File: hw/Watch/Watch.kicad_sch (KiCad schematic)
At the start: 8 parts, among them J3 Conn_01x02, J4 Conn_01x02, J5 Conn_01x02, J6 Conn_01x02

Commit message: wip
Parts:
- removed J3, J4, J5, J6: Conn_01x02, symbol Connector_Generic:Conn_01x02
- added J3: Conn_01x04, RKL-Connectors:FFC-FPC_1x04_0.5mm, symbol Connector_Generic:Conn_01x04
- added J8: Conn_01x04, RKL-Connectors:FFC-FPC_1x04_0.5mm_cable, symbol Connector_Generic:Conn_01x04
- C27, C28: footprint Capacitor_SMD:C_0402_1005Metric -> Capacitor_SMD:C_0201_0603Metric; Basic/Extended B -> E; LCSC C1523 -> C66942
- L2, L3: footprint RKL-Inductors:PCB_coil -> RKL-Inductors:PCB_coil_linear_N24
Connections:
- net MainBoard/LC-0A: now also J3.1 (Pin_1)
- net MainBoard/LC-0B: now also J3.2 (Pin_2)
- net MainBoard/LC-1A: now also J3.3 (Pin_3)
- net MainBoard/LC-1B: now also J3.4 (Pin_4)
- net at L3.1: now also J8.3 (Pin_3)
- net at L3.2: now also J8.4 (Pin_4)
- net at L2.1: now also J8.1 (Pin_1)
- net at L2.2: now also J8.2 (Pin_2)
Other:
- moved on the sheet: C27, C28, L2, L3

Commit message: PCB
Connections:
- net at L3.1: now also J8.2 (Pin_2); no longer J8.3 (Pin_3)
- net at L3.2: now also J8.1 (Pin_1); no longer J8.4 (Pin_4)
- net at L2.1: now also J8.4 (Pin_4); no longer J8.1 (Pin_1)
- net at L2.2: now also J8.3 (Pin_3); no longer J8.2 (Pin_2)
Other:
- moved on the sheet: L2, L3
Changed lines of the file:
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@@
     )
   )
-  (symbol (lib_id "Device:L") (at 99.06 97.79 0) (mirror y) (unit 1)
+  (symbol (lib_id "Device:L") (at 99.06 82.55 180) (unit 1)
     (in_bom yes) (on_board yes) (dnp no)
-    (property "Reference" "L3" (at 100.33 96.52 0)
+    (property "Reference" "L3" (at 100.33 83.82 0)
       (effects (font (size 1.27 1.27)) (justify right))
     )
-    (property "Value" "L" (at 100.33 99.06 0)
+    (property "Value" "L" (at 100.33 81.28 0)
       (effects (font (size 1.27 1.27)) (justify right))
     )
-    (property "Footprint" "RKL-Inductors:PCB_coil_linear_N24" (at 99.06 97.79 0)
+    (property "Footprint" "RKL-Inductors:PCB_coil_linear_N24" (at 99.06 82.55 0)
       (effects (font (size 1.27 1.27)) hide)
     )
-    (property "Datasheet" "~" (at 99.06 97.79 0)
+    (property "Datasheet" "~" (at 99.06 82.55 0)
       (effects (font (size 1.27 1.27)) hide)
     )
-    (property "JLCPCB_IGNORE" "ignore" (at 99.06 97.79 0)
+    (property "JLCPCB_IGNORE" "ignore" (at 99.06 82.55 0)
       (effects (font (size 1.27 1.27)) hide)
     )
@@
     )
   )
-  (symbol (lib_id "Device:L") (at 99.06 82.55 0) (mirror y) (unit 1)
+  (symbol (lib_id "Device:L") (at 99.06 97.79 180) (unit 1)
     (in_bom yes) (on_board yes) (dnp no)
-    (property "Reference" "L2" (at 100.33 81.28 0)
+    (property "Reference" "L2" (at 100.33 99.06 0)
       (effects (font (size 1.27 1.27)) (justify right))
     )
-    (property "Value" "L" (at 100.33 83.82 0)
+    (property "Value" "L" (at 100.33 96.52 0)
       (effects (font (size 1.27 1.27)) (justify right))
     )
-    (property "Footprint" "RKL-Inductors:PCB_coil_linear_N24" (at 99.06 82.55 0)
+    (property "Footprint" "RKL-Inductors:PCB_coil_linear_N24" (at 99.06 97.79 0)
       (effects (font (size 1.27 1.27)) hide)
     )
-    (property "Datasheet" "~" (at 99.06 82.55 0)
+    (property "Datasheet" "~" (at 99.06 97.79 0)
       (effects (font (size 1.27 1.27)) hide)
     )
-    (property "JLCPCB_IGNORE" "ignore" (at 99.06 82.55 0)
+    (property "JLCPCB_IGNORE" "ignore" (at 99.06 97.79 0)
       (effects (font (size 1.27 1.27)) hide)
     )

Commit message: PCB v0.0.0
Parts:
- renumbered L3 to L1
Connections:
- net L1B: now reaches J8.2 (Pin_2), L1.1
- net L1A: now reaches J8.1 (Pin_1), L1.2
- net L2B: now reaches J8.4 (Pin_4), L2.1
- net L2A: now reaches J8.3 (Pin_3), L2.2
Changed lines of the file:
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@@
     (effects (font (size 1.5 1.5) (thickness 0.3) bold) (justify left bottom))
+  )
+  (label "L1B" (at 107.95 88.9 0) (fields_autoplaced)
+    (effects (font (size 1.27 1.27)) (justify left bottom))
+  )
+  (label "L1A" (at 107.95 86.36 0) (fields_autoplaced)
+    (effects (font (size 1.27 1.27)) (justify left bottom))
+  )
+  (label "L2A" (at 107.95 91.44 0) (fields_autoplaced)
+    (effects (font (size 1.27 1.27)) (justify left bottom))
+  )
+  (label "L2B" (at 107.95 93.98 0) (fields_autoplaced)
+    (effects (font (size 1.27 1.27)) (justify left bottom))
   )
   (symbol (lib_id "Connector_Generic:Conn_01x04") (at 124.46 88.9 0) (mirror y) (unit 1)
@@
   (symbol (lib_id "Device:L") (at 99.06 82.55 180) (unit 1)
     (in_bom yes) (on_board yes) (dnp no)
-    (property "Reference" "L3" (at 100.33 83.82 0)
+    (property "Reference" "L1" (at 100.33 83.82 0)
       (effects (font (size 1.27 1.27)) (justify right))
     )
@@
       (project "Watch"
         (path "/1db6f6a7-b341-422f-8dcc-b4fd8e3ba0c0"
-          (reference "L3") (unit 1)
+          (reference "L1") (unit 1)
         )
       )

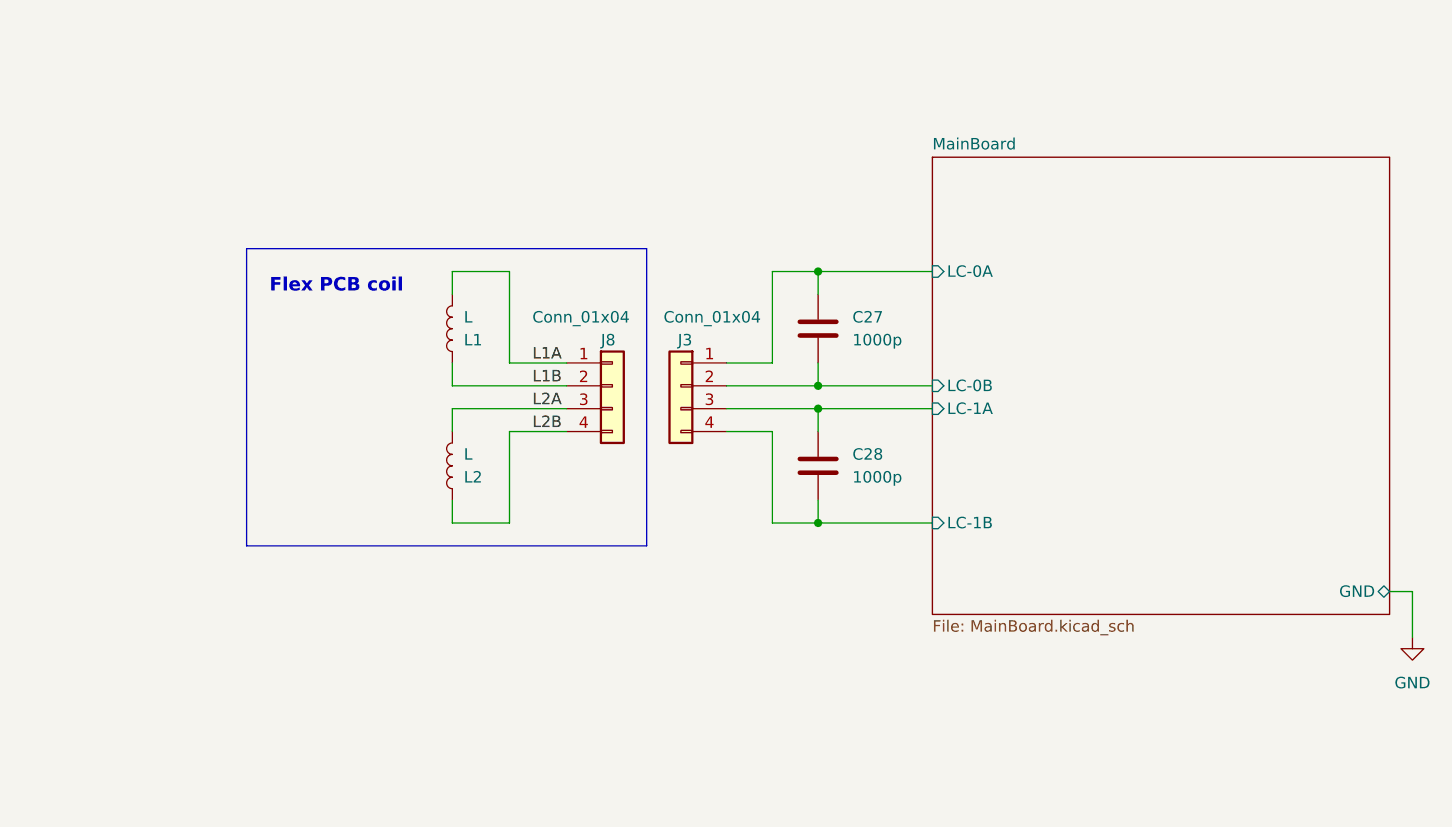
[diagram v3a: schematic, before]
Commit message: Shift LDO
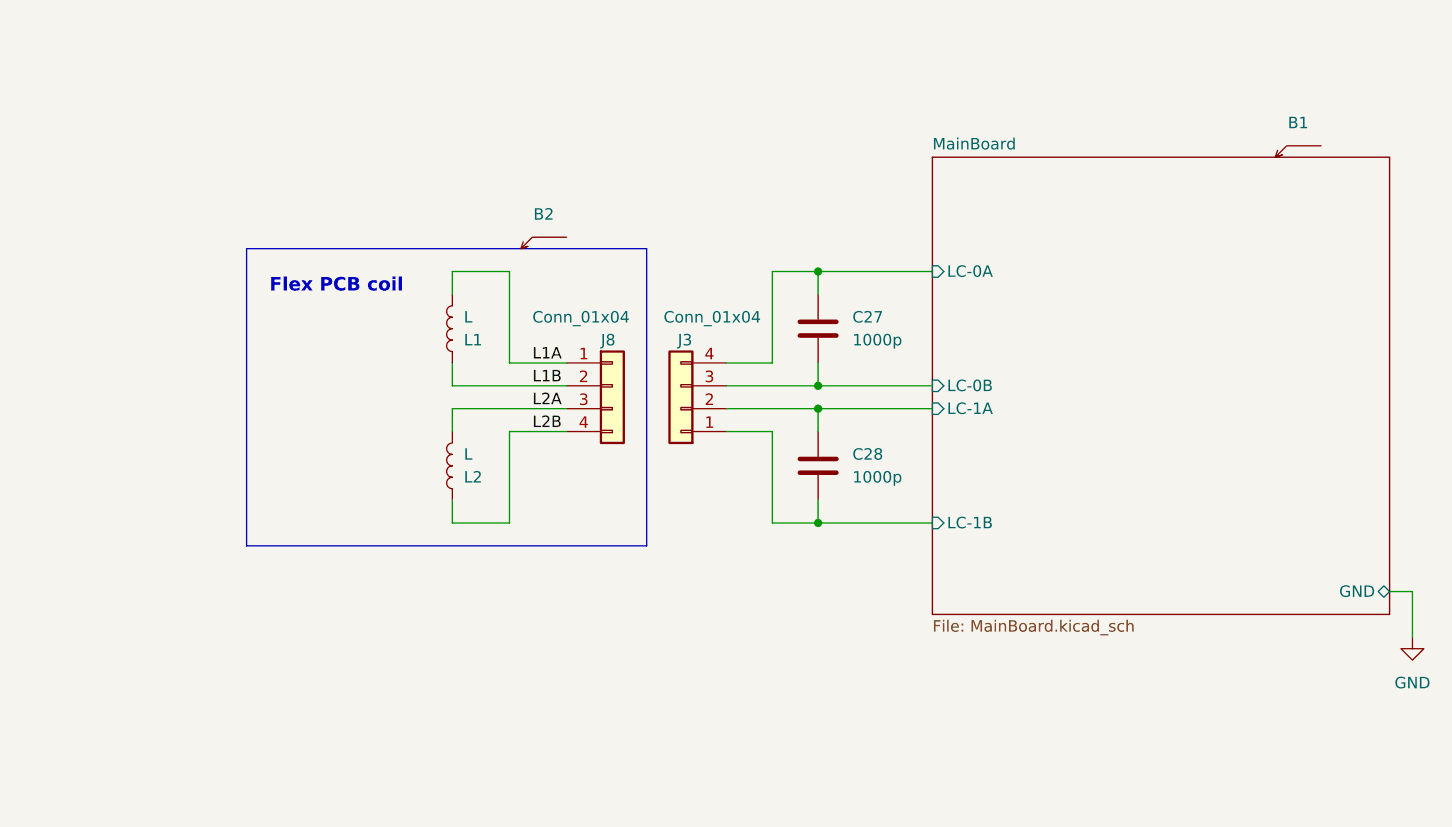
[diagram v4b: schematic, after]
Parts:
- added B1, B2: ~, RKL-AuxiliarySymbols:Board, symbol RKL-AuxiliarySymbols:Board
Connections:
- net MainBoard/LC-0A: now also J3.4 (Pin_4); no longer J3.1 (Pin_1)
- net MainBoard/LC-0B: now also J3.3 (Pin_3); no longer J3.2 (Pin_2)
- net MainBoard/LC-1A: now also J3.2 (Pin_2); no longer J3.3 (Pin_3)
- net MainBoard/LC-1B: now also J3.1 (Pin_1); no longer J3.4 (Pin_4)
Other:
- moved on the sheet: J3
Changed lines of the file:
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@@
     (effects (font (size 1.27 1.27)) (justify left bottom))
   )
-  (symbol (lib_id "Connector_Generic:Conn_01x04") (at 124.46 88.9 0) (mirror y) (unit 1)
+  (symbol (lib_id "Connector_Generic:Conn_01x04") (at 124.46 91.44 180) (unit 1)
     (in_bom yes) (on_board yes) (dnp no)
     (property "Reference" "J3" (at 125.73 83.82 0)
@@
       (effects (font (size 1.27 1.27)) (justify left))
     )
-    (property "Footprint" "RKL-Connectors:FFC-FPC_1x04_0.5mm" (at 124.46 88.9 0)
-      (effects (font (size 1.27 1.27)) hide)
-    )
-    (property "Datasheet" "~" (at 124.46 88.9 0)
+    (property "Footprint" "RKL-Connectors:FFC-FPC_1x04_0.5mm" (at 124.46 91.44 0)
+      (effects (font (size 1.27 1.27)) hide)
+    )
+    (property "Datasheet" "~" (at 124.46 91.44 0)
       (effects (font (size 1.27 1.27)) hide)
     )
@@
         (path "/1db6f6a7-b341-422f-8dcc-b4fd8e3ba0c0"
           (reference "J3") (unit 1)
+        )
+      )
+    )
+  )
+  (symbol (lib_id "RKL-AuxiliarySymbols:Board") (at 106.68 73.66 0) (unit 1)
+    (in_bom yes) (on_board yes) (dnp no) (fields_autoplaced)
+    (property "Reference" "B2" (at 109.22 69.85 0)
+      (effects (font (size 1.27 1.27)))
+    )
+    (property "Value" "~" (at 106.68 73.66 0)
+      (effects (font (size 1.27 1.27)))
+    )
+    (property "Footprint" "RKL-AuxiliarySymbols:Board" (at 109.22 68.58 0)
+      (effects (font (size 1.27 1.27)) hide)
+    )
+    (property "Datasheet" "" (at 106.68 73.66 0)
+      (effects (font (size 1.27 1.27)) hide)
+    )
+    (instances
+      (project "Watch"
+        (path "/1db6f6a7-b341-422f-8dcc-b4fd8e3ba0c0"
+          (reference "B2") (unit 1)
         )
       )
@@
         )
       )
+    )
+  )
+  (symbol (lib_id "RKL-AuxiliarySymbols:Board") (at 190.5 63.5 0) (unit 1)
+    (in_bom yes) (on_board yes) (dnp no) (fields_autoplaced)
+    (property "Reference" "B1" (at 193.04 59.69 0)
+      (effects (font (size 1.27 1.27)))
+    )
+    (property "Value" "~" (at 190.5 63.5 0)
+      (effects (font (size 1.27 1.27)))
+    )
+    (property "Footprint" "RKL-AuxiliarySymbols:Board" (at 193.04 58.42 0)
+      (effects (font (size 1.27 1.27)) hide)
+    )
+    (property "Datasheet" "" (at 190.5 63.5 0)
+      (effects (font (size 1.27 1.27)) hide)
+    )
+    (instances
+      (project "Watch"
+        (path "/1db6f6a7-b341-422f-8dcc-b4fd8e3ba0c0"
+          (reference "B1") (unit 1)
+        )
+      )

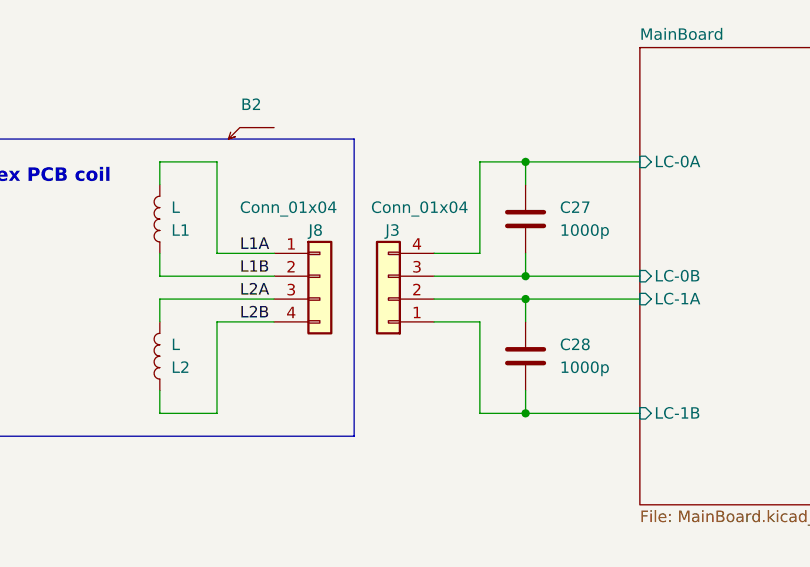
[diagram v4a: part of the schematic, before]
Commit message: Shift flex connector
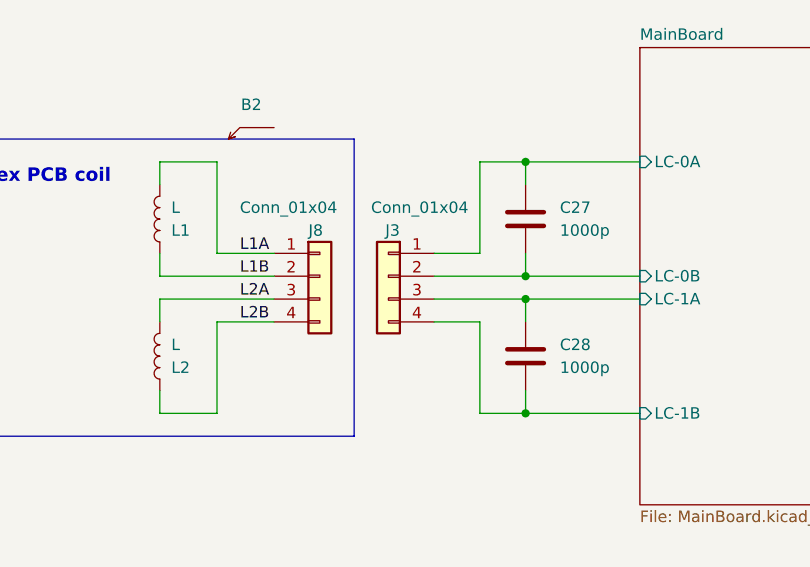
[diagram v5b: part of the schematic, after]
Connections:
- net MainBoard/LC-0A: now also J3.1 (Pin_1); no longer J3.4 (Pin_4)
- net MainBoard/LC-0B: now also J3.2 (Pin_2); no longer J3.3 (Pin_3)
- net MainBoard/LC-1A: now also J3.3 (Pin_3); no longer J3.2 (Pin_2)
- net MainBoard/LC-1B: now also J3.4 (Pin_4); no longer J3.1 (Pin_1)
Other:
- moved on the sheet: J3
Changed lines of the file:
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@@
     (effects (font (size 1.27 1.27)) (justify left bottom))
   )
-  (symbol (lib_id "Connector_Generic:Conn_01x04") (at 124.46 91.44 180) (unit 1)
+  (symbol (lib_id "Connector_Generic:Conn_01x04") (at 124.46 88.9 0) (mirror y) (unit 1)
     (in_bom yes) (on_board yes) (dnp no)
     (property "Reference" "J3" (at 125.73 83.82 0)
@@
       (effects (font (size 1.27 1.27)) (justify left))
     )
-    (property "Footprint" "RKL-Connectors:FFC-FPC_1x04_0.5mm" (at 124.46 91.44 0)
+    (property "Footprint" "RKL-Connectors:FFC-FPC_1x04_0.5mm" (at 124.46 88.9 0)
       (effects (font (size 1.27 1.27)) hide)
     )
-    (property "Datasheet" "~" (at 124.46 91.44 0)
+    (property "Datasheet" "~" (at 124.46 88.9 0)
       (effects (font (size 1.27 1.27)) hide)
     )
